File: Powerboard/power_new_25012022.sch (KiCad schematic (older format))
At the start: 9 parts

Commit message: 01022022
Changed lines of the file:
@@
 F1 "battchrg.sch" 50
 F2 "System" I R 3300 3150 50
+F3 "Stat1" I L 2450 3050 50
+F4 "Stat2" I L 2450 3150 50
+F5 "PG" I L 2450 3250 50
 $EndSheet
 $Comp

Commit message: 08/02/2022 start
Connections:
- net labels added: 3.3STAT1, 3.3STAT2, BATTSTAT1, BATTSTAT2, PG
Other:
- moved on the sheet: D?, J?, P?, Q?, R?, U?
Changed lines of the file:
@@
 L power:GND #PWR?
 U 1 1 61C7C50B
-P 500 2600
-F 0 "#PWR?" H 500 2350 50  0001 C CNN
-F 1 "GND" H 505 2427 50  0000 C CNN
-F 2 "" H 500 2600 50  0001 C CNN
-F 3 "" H 500 2600 50  0001 C CNN
-	1    500  2600
+P 950 3100
+F 0 "#PWR?" H 950 2850 50  0001 C CNN
+F 1 "GND" H 955 2927 50  0000 C CNN
+F 2 "" H 950 3100 50  0001 C CNN
+F 3 "" H 950 3100 50  0001 C CNN
+	1    950  3100
 	1    0    0    -1
 $EndComp
@@
 L Connector:USB_C_Plug_USB2.0 P?
 U 1 1 61C7C511
-P 500 1300
-F 0 "P?" H 607 2167 50  0000 C CNN
-F 1 "USB_C_Plug_USB2.0" H 607 2076 50  0000 C CNN
-F 2 "" H 650 1300 50  0001 C CNN
-F 3 "https://www.usb.org/sites/default/files/documents/usb_type-c.zip" H 650 1300 50  0001 C CNN
-	1    500  1300
-	1    0    0    -1
-$EndComp
-Wire Wire Line
-	1100 1400 1950 1400
-Wire Wire Line
-	1100 1200 1400 1200
-Wire Wire Line
-	1400 1200 1400 1500
-Wire Wire Line
-	1400 1500 1850 1500
-Wire Wire Line
-	200  2400 500  2400
-Wire Wire Line
-	500  2400 500  2600
-Connection ~ 500  2400
-Wire Wire Line
-	1650 700  1650 1000
-Wire Wire Line
-	1650 1000 1750 1000
+P 950 1800
+F 0 "P?" H 1057 2667 50  0000 C CNN
+F 1 "USB_C_Plug_USB2.0" H 1057 2576 50  0000 C CNN
+F 2 "" H 1100 1800 50  0001 C CNN
+F 3 "https://www.usb.org/sites/default/files/documents/usb_type-c.zip" H 1100 1800 50  0001 C CNN
+	1    950  1800
+	1    0    0    -1
+$EndComp
+Wire Wire Line
+	1550 1900 2400 1900
+Wire Wire Line
+	1550 1700 1850 1700
+Wire Wire Line
+	1850 1700 1850 2000
+Wire Wire Line
+	1850 2000 2300 2000
+Wire Wire Line
+	650  2900 950  2900
+Wire Wire Line
+	950  2900 950  3100
+Connection ~ 950  2900
+Wire Wire Line
+	2100 1200 2100 1500
+Wire Wire Line
+	2100 1500 2200 1500
 $Comp
 L Device:R_Small R?
 U 1 1 61C7C520
-P 1300 1000
-F 0 "R?" V 1104 1000 50  0000 C CNN
-F 1 "22K" V 1195 1000 50  0000 C CNN
-F 2 "" H 1300 1000 50  0001 C CNN
-F 3 "~" H 1300 1000 50  0001 C CNN
-	1    1300 1000
+P 1750 1500
+F 0 "R?" V 1554 1500 50  0000 C CNN
+F 1 "22K" V 1645 1500 50  0000 C CNN
+F 2 "" H 1750 1500 50  0001 C CNN
+F 3 "~" H 1750 1500 50  0001 C CNN
+	1    1750 1500
 	0    1    1    0
 $EndComp
 Wire Wire Line
-	1100 900  1100 1000
-Wire Wire Line
-	1100 1000 1200 1000
-Connection ~ 1100 1000
+	1550 1400 1550 1500
+Wire Wire Line
+	1550 1500 1650 1500
+Connection ~ 1550 1500
 $Comp
 L power:GND #PWR?
 U 1 1 61C7C529
-P 1500 1100
-F 0 "#PWR?" H 1500 850 50  0001 C CNN
-F 1 "GND" H 1505 927 50  0000 C CNN
-F 2 "" H 1500 1100 50  0001 C CNN
-F 3 "" H 1500 1100 50  0001 C CNN
-	1    1500 1100
-	1    0    0    -1
-$EndComp
-Wire Wire Line
-	1400 1000 1500 1000
-Wire Wire Line
-	1500 1000 1500 1100
-Wire Wire Line
-	1100 700  1650 700
-Wire Wire Line
-	200  2200 200  2400
-Wire Wire Line
-	500  2200 500  2400
+P 1950 1600
+F 0 "#PWR?" H 1950 1350 50  0001 C CNN
+F 1 "GND" H 1955 1427 50  0000 C CNN
+F 2 "" H 1950 1600 50  0001 C CNN
+F 3 "" H 1950 1600 50  0001 C CNN
+	1    1950 1600
+	1    0    0    -1
+$EndComp
+Wire Wire Line
+	1850 1500 1950 1500
+Wire Wire Line
+	1950 1500 1950 1600
+Wire Wire Line
+	1550 1200 2100 1200
+Wire Wire Line
+	650  2700 650  2900
+Wire Wire Line
+	950  2700 950  2900
 $Comp
 L Interface_USB:CP2102N-A01-GQFN24 U?
 U 1 1 61C8AC6C
-P 2700 1000
-F 0 "U?" H 2700 2081 50  0000 C CNN
-F 1 "CP2102N-A01-GQFN24" H 2700 1990 50  0000 C CNN
-F 2 "Package_DFN_QFN:QFN-24-1EP_4x4mm_P0.5mm_EP2.6x2.6mm" H 3150 200 50  0001 L CNN
-F 3 "https://www.silabs.com/documents/public/data-sheets/cp2102n-datasheet.pdf" H 2750 -50 50  0001 C CNN
-	1    2700 1000
-	1    0    0    -1
-$EndComp
-Wire Wire Line
-	1900 1300 2100 1300
+P 3150 1500
+F 0 "U?" H 3150 2581 50  0000 C CNN
+F 1 "CP2102N-A01-GQFN24" H 3150 2490 50  0000 C CNN
+F 2 "Package_DFN_QFN:QFN-24-1EP_4x4mm_P0.5mm_EP2.6x2.6mm" H 3600 700 50  0001 L CNN
+F 3 "https://www.silabs.com/documents/public/data-sheets/cp2102n-datasheet.pdf" H 3200 450 50  0001 C CNN
+	1    3150 1500
+	1    0    0    -1
+$EndComp
+Wire Wire Line
+	2350 1800 2550 1800
 $Comp
 L Power_Protection:SP0503BAHT D?
 U 1 1 61C8AC77
-P 1850 2050
-F 0 "D?" H 2055 2096 50  0000 L CNN
-F 1 "SP0503BAHT" H 2055 2005 50  0000 L CNN
-F 2 "Package_TO_SOT_SMD:SOT-143" H 2075 2000 50  0001 L CNN
-F 3 "http://www.littelfuse.com/~/media/files/littelfuse/technical%20resources/documents/data%20sheets/sp05xxba.pdf" H 1975 2175 50  0001 C CNN
-	1    1850 2050
-	1    0    0    -1
-$EndComp
-Wire Wire Line
-	1750 1850 1750 1000
-Connection ~ 1750 1000
-Wire Wire Line
-	1750 1000 2100 1000
-Wire Wire Line
-	1850 1850 1850 1500
-Connection ~ 1850 1500
-Wire Wire Line
-	1850 1500 2100 1500
-Wire Wire Line
-	1950 1850 1950 1400
-Connection ~ 1950 1400
-Wire Wire Line
-	1950 1400 2100 1400
+P 2300 2550
+F 0 "D?" H 2505 2596 50  0000 L CNN
+F 1 "SP0503BAHT" H 2505 2505 50  0000 L CNN
+F 2 "Package_TO_SOT_SMD:SOT-143" H 2525 2500 50  0001 L CNN
+F 3 "http://www.littelfuse.com/~/media/files/littelfuse/technical%20resources/documents/data%20sheets/sp05xxba.pdf" H 2425 2675 50  0001 C CNN
+	1    2300 2550
+	1    0    0    -1
+$EndComp
+Wire Wire Line
+	2200 2350 2200 1500
+Connection ~ 2200 1500
+Wire Wire Line
+	2200 1500 2550 1500
+Wire Wire Line
+	2300 2350 2300 2000
+Connection ~ 2300 2000
+Wire Wire Line
+	2300 2000 2550 2000
+Wire Wire Line
+	2400 2350 2400 1900
+Connection ~ 2400 1900
+Wire Wire Line
+	2400 1900 2550 1900
 $Comp
 L power:GND #PWR?
 U 1 1 61C8AC86
-P 2800 2000
-F 0 "#PWR?" H 2800 1750 50  0001 C CNN
-F 1 "GND" H 2805 1827 50  0000 C CNN
-F 2 "" H 2800 2000 50  0001 C CNN
-F 3 "" H 2800 2000 50  0001 C CNN
-	1    2800 2000
-	1    0    0    -1
-$EndComp
-Wire Wire Line
-	2700 2000 2800 2000
-Wire Wire Line
-	2800 1900 2800 2000
-Connection ~ 2800 2000
-Wire Wire Line
-	2700 1900 2700 2000
-Connection ~ 2700 2000
-Wire Wire Line
-	2700 2000 2700 2100
-Wire Wire Line
-	2800 2000 2800 2100
-Wire Wire Line
-	1850 2250 1850 2450
+P 3250 2500
+F 0 "#PWR?" H 3250 2250 50  0001 C CNN
+F 1 "GND" H 3255 2327 50  0000 C CNN
+F 2 "" H 3250 2500 50  0001 C CNN
+F 3 "" H 3250 2500 50  0001 C CNN
+	1    3250 2500
+	1    0    0    -1
+$EndComp
+Wire Wire Line
+	3150 2500 3250 2500
+Wire Wire Line
+	3250 2400 3250 2500
+Connection ~ 3250 2500
+Wire Wire Line
+	3150 2400 3150 2500
+Connection ~ 3150 2500
+Wire Wire Line
+	3150 2500 3150 2600
+Wire Wire Line
+	3250 2500 3250 2600
+Wire Wire Line
+	2300 2750 2300 2950
 $Sheet
-S 2450 3000 850  300
+S 3900 4050 850  300
 U 61BEB629
 F0 "battery Charger" 50
 F1 "battchrg.sch" 50
-F2 "System" I R 3300 3150 50
-F3 "Stat1" I L 2450 3050 50
-F4 "Stat2" I L 2450 3150 50
-F5 "PG" I L 2450 3250 50
+F2 "System" I R 4750 4200 50
+F3 "Stat1" I L 3900 4100 50
+F4 "Stat2" I L 3900 4200 50
+F5 "PG" I L 3900 4300 50
 $EndSheet
 $Comp
 L Transistor_FET:IRF6728M Q?
 U 1 1 61C4D11C
-P 3800 3950
-F 0 "Q?" H 4004 3996 50  0000 L CNN
-F 1 "IRF6728M" H 4004 3905 50  0000 L CNN
-F 2 "Package_DirectFET:DirectFET_MX" H 3800 3950 50  0001 C CIN
-F 3 "https://www.infineon.com/dgdl/irf6728mpbf.pdf?fileId=5546d462533600a4015355ed73701a9c" H 3800 3950 50  0001 L CNN
-	1    3800 3950
+P 5250 5000
+F 0 "Q?" H 5454 5046 50  0000 L CNN
+F 1 "IRF6728M" H 5454 4955 50  0000 L CNN
+F 2 "Package_DirectFET:DirectFET_MX" H 5250 5000 50  0001 C CIN
+F 3 "https://www.infineon.com/dgdl/irf6728mpbf.pdf?fileId=5546d462533600a4015355ed73701a9c" H 5250 5000 50  0001 L CNN
+	1    5250 5000
 	-1   0    0    1
 $EndComp
@@
 L Transistor_FET:IRF6728M Q?
 U 1 1 61C4D116
-P 3800 3550
-F 0 "Q?" H 4004 3596 50  0000 L CNN
-F 1 "IRF6728M" H 4004 3505 50  0000 L CNN
-F 2 "Package_DirectFET:DirectFET_MX" H 3800 3550 50  0001 C CIN
-F 3 "https://www.infineon.com/dgdl/irf6728mpbf.pdf?fileId=5546d462533600a4015355ed73701a9c" H 3800 3550 50  0001 L CNN
-	1    3800 3550
+P 5250 4600
+F 0 "Q?" H 5454 4646 50  0000 L CNN
+F 1 "IRF6728M" H 5454 4555 50  0000 L CNN
+F 2 "Package_DirectFET:DirectFET_MX" H 5250 4600 50  0001 C CIN
+F 3 "https://www.infineon.com/dgdl/irf6728mpbf.pdf?fileId=5546d462533600a4015355ed73701a9c" H 5250 4600 50  0001 L CNN
+	1    5250 4600
 	-1   0    0    1
 $EndComp
@@
 Text Label 10550 2550 0    50   ~ 0
 LPC
-Text Label 4000 3550 0    50   ~ 0
+Text Label 5450 4600 0    50   ~ 0
 LPC
 Wire Wire Line
-	3700 3350 3700 3150
-Wire Wire Line
-	3700 3150 3300 3150
+	5150 4400 5150 4200
+Wire Wire Line
+	5150 4200 4750 4200
 $Comp
 L Connector:Conn_01x01_Female J?
 U 1 1 61F29D49
-P 4200 3950
-F 0 "J?" H 4228 3976 50  0000 L CNN
-F 1 "Conn_01x01_Female" H 4228 3885 50  0000 L CNN
-F 2 "" H 4200 3950 50  0001 C CNN
-F 3 "~" H 4200 3950 50  0001 C CNN
-	1    4200 3950
+P 5650 5000
+F 0 "J?" H 5678 5026 50  0000 L CNN
+F 1 "Conn_01x01_Female" H 5678 4935 50  0000 L CNN
+F 2 "" H 5650 5000 50  0001 C CNN
+F 3 "~" H 5650 5000 50  0001 C CNN
+	1    5650 5000
 	1    0    0    -1
 $EndComp
@@
 CAN_RX
 $Sheet
-S 4350 3000 750  350
+S 5800 4050 750  350
 U 61F04C1A
 F0 "3.3redundant" 50
 F1 "3.sch" 50
-F2 "Vin" I L 4350 3150 50
+F2 "Vin" I L 5800 4200 50
+F3 "Vout" I R 6550 4350 50
+F4 "STAT1" I R 6550 4250 50
+F5 "STAT2" I R 6550 4150 50
 $EndSheet
-Connection ~ 3700 3150
-Wire Wire Line
-	3700 3150 4350 3150
+Connection ~ 5150 4200
+Wire Wire Line
+	5150 4200 5800 4200
+Text Label 6550 4150 0    50   ~ 0
+3.3STAT2
+Text Label 10550 2650 0    50   ~ 0
+3.3STAT2
+Text Label 10550 2750 0    50   ~ 0
+3.3STAT1
+Text Label 6550 4250 0    50   ~ 0
+3.3STAT1
+Text Label 3900 4100 2    50   ~ 0
+BATTSTAT1
+Text Label 3900 4200 2    50   ~ 0
+BATTSTAT2
+Text Label 3900 4300 2    50   ~ 0
+PG
+Text Label 8950 3050 2    50   ~ 0
+BATTSTAT1
+Text Label 8950 2950 2    50   ~ 0
+BATTSTAT2
+Text Label 10550 2850 0    50   ~ 0
+PG
 $EndSCHEMATC

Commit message: 08/02/2022 update3
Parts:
- added 24vEnableDiode: LED, symbol Device:LED
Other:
- moved on the sheet: J?
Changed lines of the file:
@@
 L Connector:Conn_01x01_Female J?
 U 1 1 61F29D49
-P 5650 5000
-F 0 "J?" H 5678 5026 50  0000 L CNN
-F 1 "Conn_01x01_Female" H 5678 4935 50  0000 L CNN
-F 2 "" H 5650 5000 50  0001 C CNN
-F 3 "~" H 5650 5000 50  0001 C CNN
-	1    5650 5000
+P 5950 5000
+F 0 "J?" H 5978 5026 50  0000 L CNN
+F 1 "Conn_01x01_Female" H 5978 4935 50  0000 L CNN
+F 2 "" H 5950 5000 50  0001 C CNN
+F 3 "~" H 5950 5000 50  0001 C CNN
+	1    5950 5000
 	1    0    0    -1
 $EndComp
@@
 Text Label 10550 2850 0    50   ~ 0
 PG
+$Comp
+L Device:LED 24vEnableDiode
+U 1 1 6208CC45
+P 5600 5000
+F 0 "24vEnableDiode" H 5593 5217 50  0000 C CNN
+F 1 "LED" H 5593 5126 50  0000 C CNN
+F 2 "" H 5600 5000 50  0001 C CNN
+F 3 "~" H 5600 5000 50  0001 C CNN
+	1    5600 5000
+	1    0    0    -1
+$EndComp
 $EndSCHEMATC

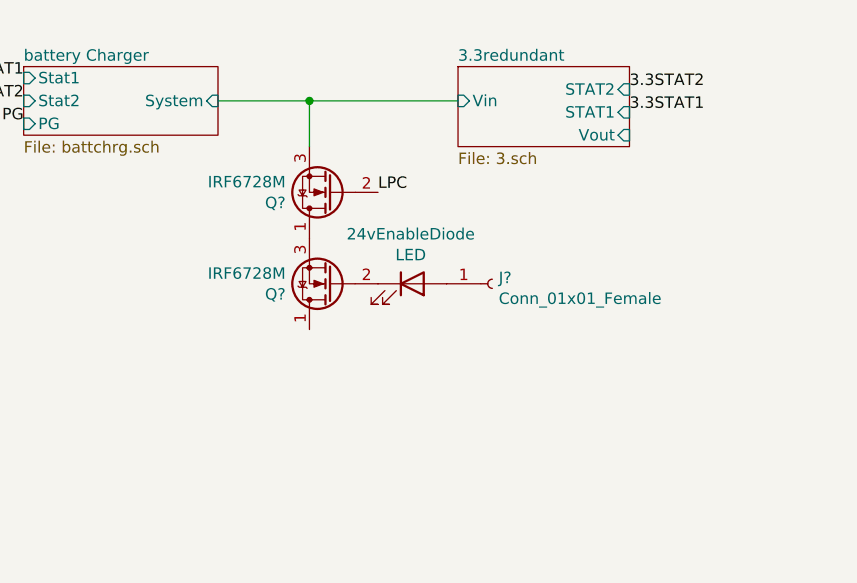
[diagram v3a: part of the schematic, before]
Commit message: reverse polarity protection
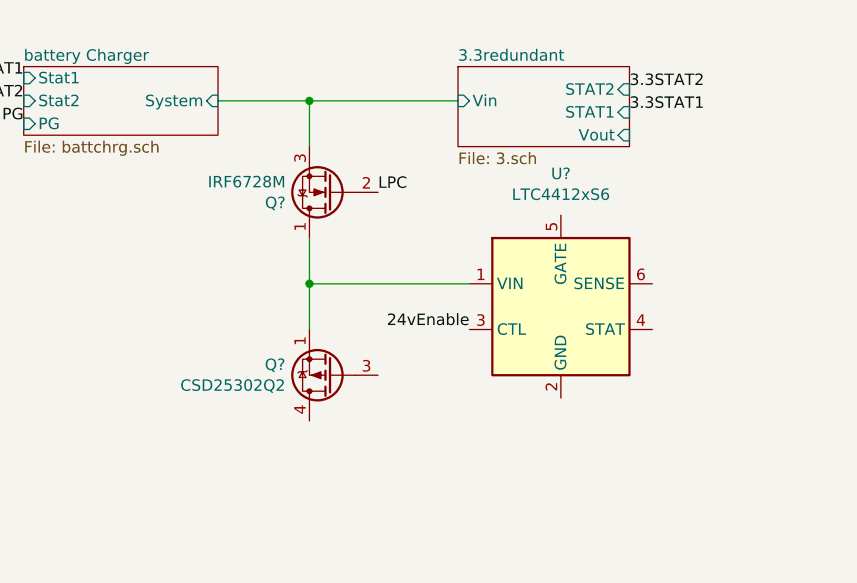
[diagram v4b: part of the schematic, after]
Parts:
- removed 24vEnableDiode: LED, symbol Device:LED
- removed J?: Conn_01x01_Female, symbol Connector:Conn_01x01_Female
- removed Q?: IRF6728M, Package_DirectFET:DirectFET_MX, symbol Transistor_FET:IRF6728M
- added Q?: CSD25302Q2, Package_SON:Texas_DQK, symbol Transistor_FET:CSD25302Q2
- added U?: LTC4412xS6, Package_TO_SOT_SMD:TSOT-23-6, symbol Power_Management:LTC4412xS6
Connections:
- net labels added: 24vEnable
- wire segments 35 -> 38
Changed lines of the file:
@@
-$Comp
-L Transistor_FET:IRF6728M Q?
-U 1 1 61C4D11C
-P 5250 5000
-F 0 "Q?" H 5454 5046 50  0000 L CNN
-F 1 "IRF6728M" H 5454 4955 50  0000 L CNN
-F 2 "Package_DirectFET:DirectFET_MX" H 5250 5000 50  0001 C CIN
-F 3 "https://www.infineon.com/dgdl/irf6728mpbf.pdf?fileId=5546d462533600a4015355ed73701a9c" H 5250 5000 50  0001 L CNN
-	1    5250 5000
-	-1   0    0    1
-$EndComp
 $Comp
 L Transistor_FET:IRF6728M Q?
@@
 Wire Wire Line
 	5150 4200 4750 4200
-$Comp
-L Connector:Conn_01x01_Female J?
-U 1 1 61F29D49
-P 5950 5000
-F 0 "J?" H 5978 5026 50  0000 L CNN
-F 1 "Conn_01x01_Female" H 5978 4935 50  0000 L CNN
-F 2 "" H 5950 5000 50  0001 C CNN
-F 3 "~" H 5950 5000 50  0001 C CNN
-	1    5950 5000
-	1    0    0    -1
-$EndComp
 Wire Wire Line
 	9100 5800 9000 5800
@@
 PG
 $Comp
-L Device:LED 24vEnableDiode
-U 1 1 6208CC45
-P 5600 5000
-F 0 "24vEnableDiode" H 5593 5217 50  0000 C CNN
-F 1 "LED" H 5593 5126 50  0000 C CNN
-F 2 "" H 5600 5000 50  0001 C CNN
-F 3 "~" H 5600 5000 50  0001 C CNN
-	1    5600 5000
+L Power_Management:LTC4412xS6 U?
+U 1 1 623ADA4B
+P 6250 5100
+F 0 "U?" H 6250 5681 50  0000 C CNN
+F 1 "LTC4412xS6" H 6250 5590 50  0000 C CNN
+F 2 "Package_TO_SOT_SMD:TSOT-23-6" H 6900 4750 50  0001 C CNN
+F 3 "https://www.analog.com/media/en/technical-documentation/data-sheets/4412fb.pdf" H 8350 4900 50  0001 C CNN
+	1    6250 5100
 	1    0    0    -1
 $EndComp
+$Comp
+L Transistor_FET:CSD25302Q2 Q?
+U 1 1 623AE1FA
+P 5150 5400
+F 0 "Q?" H 5255 5354 50  0000 L CNN
+F 1 "CSD25302Q2" H 5255 5445 50  0000 L CNN
+F 2 "Package_SON:Texas_DQK" H 5650 5250 50  0001 C CNN
+F 3 "https://www.ti.com/lit/ds/slps234b/slps234b.pdf" H 5050 5400 50  0001 C CNN
+	1    5150 5400
+	-1   0    0    1
+$EndComp
+Text Label 5850 5200 2    50   ~ 0
+24vEnable
+Wire Wire Line
+	5150 4800 5150 5000
+Wire Wire Line
+	5150 5000 5850 5000
+Connection ~ 5150 5000
+Wire Wire Line
+	5150 5000 5150 5200
 $EndSCHEMATC
